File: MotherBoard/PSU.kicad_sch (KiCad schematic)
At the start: 49 parts, among them U401 LMR51430, U402 LMR51430

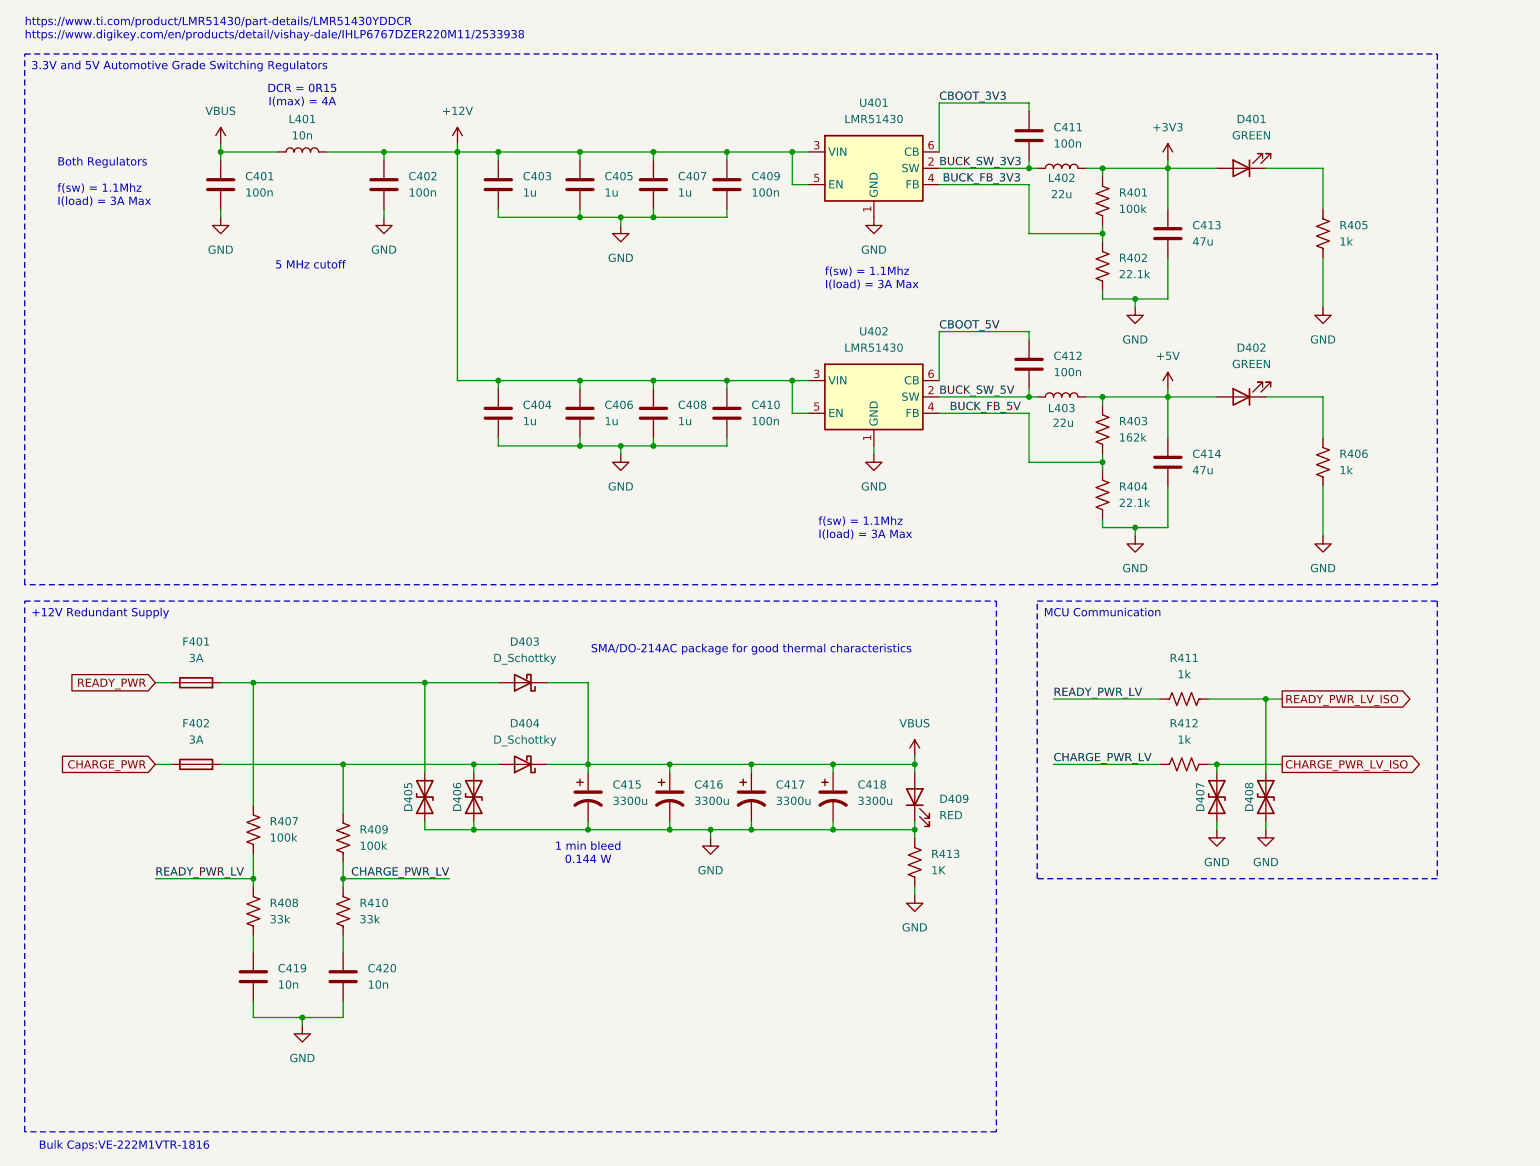
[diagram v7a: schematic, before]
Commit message: Completed BOM except inductors
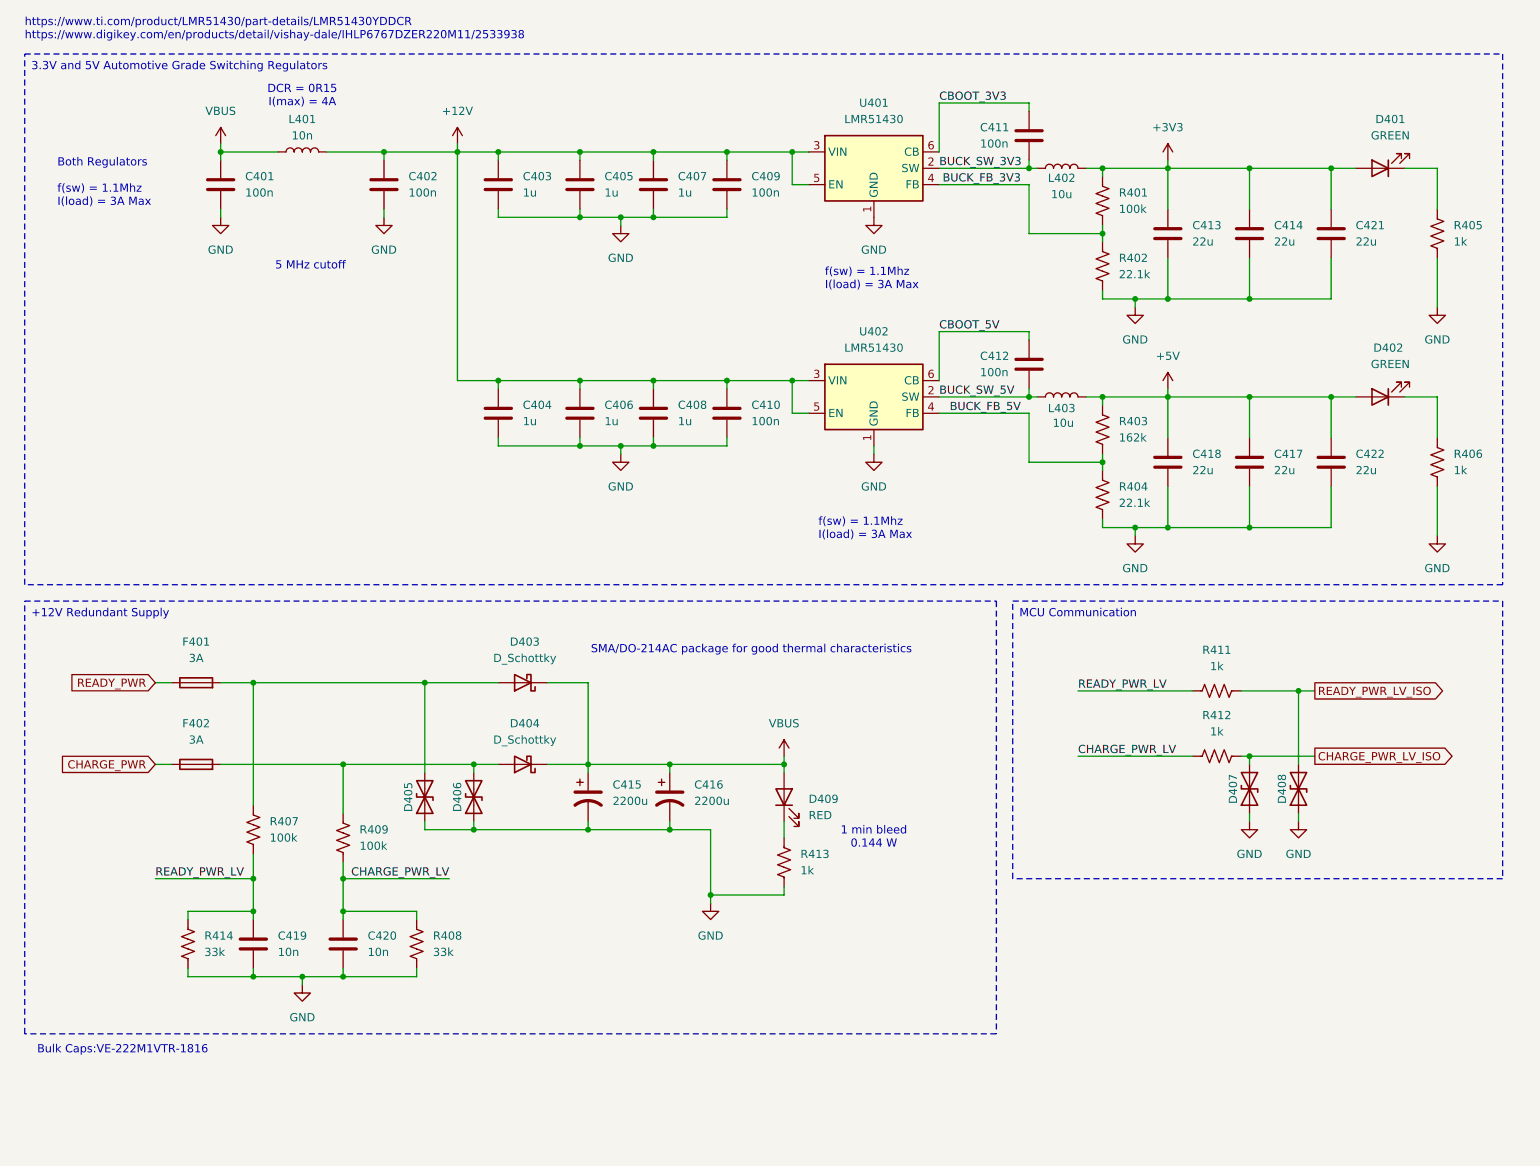
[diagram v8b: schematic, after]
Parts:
- removed C417, C418: 3300u, Capacitor_SMD:CP_Elec_18x17.5, symbol Device:C_Polarized_US
- removed R410: 33k, Resistor_SMD:R_0402_1005Metric, symbol Device:R_US
- added C417, C418, C421, C422: 22u, Capacitor_SMD:C_0805_2012Metric, symbol Device:C
- added R414: 33k, Resistor_SMD:R_0402_1005Metric, symbol Device:R_US
- C401, C402, C411, C412: Manufacturer_Part_Number (none) -> CL05B104KO5NNNC
- C403, C404, C405, C406, C407, C408: footprint Capacitor_SMD:C_0402_1005Metric -> Capacitor_SMD:C_0805_2012Metric; Manufacturer_Part_Number (none) -> CL21B105KBFNNNE
- C409, C410: footprint Capacitor_SMD:C_0402_1005Metric -> Capacitor_SMD:C_0603_1608Metric; Manufacturer_Part_Number (none) -> CC0603KRX7R9BB104
- C413, C414: value 47u -> 22u; footprint Capacitor_SMD:C_0402_1005Metric -> Capacitor_SMD:C_0805_2012Metric; Manufacturer_Part_Number (none) -> CL21A226MAQNNNE
- C415, C416: value 3300u -> 2200u; Manufacturer_Part_Number (none) -> VE-222M1VTR-1816
- C419, C420: Manufacturer_Part_Number (none) -> CC0402KRX7R9BB103
- D401, D402: Manufacturer_Part_Number (none) -> VLMTG1401-GS08
- D409: Manufacturer_Part_Number (none) -> KT-0603R
- L401: footprint Capacitor_SMD:C_0402_1005Metric -> (none)
- L402, L403: value 22u -> 10u; footprint Inductor_SMD:L_Changjiang_FNR6045S -> (none); Manufacturer_Part_Number FNR6045S220MT -> (none)
- R401, R407, R409: Manufacturer_Part_Number (none) -> 0402WGF1003TCE
- R402, R404: Manufacturer_Part_Number (none) -> 0402WGF2212TCE
- R403: Manufacturer_Part_Number (none) -> FRC0402F1623TS
- R405, R406: Manufacturer_Part_Number (none) -> 0402WGF1001TCE
- R408: Manufacturer_Part_Number (none) -> 0402WGF3302TCE
- R411, R412: footprint Resistor_SMD:R_0402_1005Metric -> Resistor_SMD:R_2512_6332Metric; Manufacturer_Part_Number (none) -> FRC2512J102 TS
- R413: value 1K -> 1k; footprint Resistor_SMD:R_0402_1005Metric -> Resistor_SMD:R_2512_6332Metric; Manufacturer_Part_Number (none) -> FRC2512J102 TS
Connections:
- net +3V3: now also C414.1, C421.1
- net +5V: now also C417.1, C418.1, C422.1; no longer C414.1
- net CHARGE_PWR_LV: now also C420.1, R408.1
- net GND: now also R408.2, C417.2, C418.2, C421.2, C422.2, R414.2; no longer D409.1 (K), R413.1
- net READY_PWR_LV: now also C419.1, R414.1; no longer R408.1
- new net: D409.1 (K), R413.1
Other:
- moved on the sheet: C419, C420, D401, D407, D408, D409, R405, R411, R412, R413
